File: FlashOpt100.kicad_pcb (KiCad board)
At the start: 2 copper layers, 16 x 38 mm, 8 parts, among them J1 Tandy_100_102_200_option_rom, J2 29C256, U1 29F010

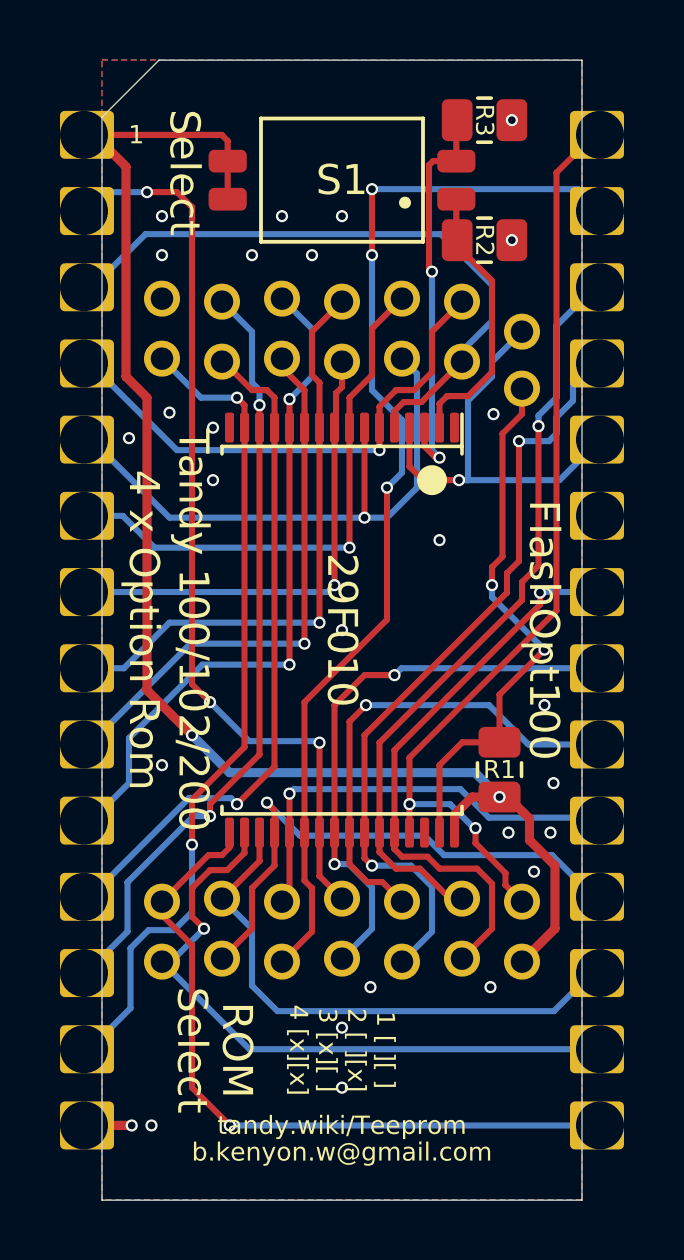
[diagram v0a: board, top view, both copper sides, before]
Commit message: adjust some footprints and remove flashopt100 programming adapter from readme
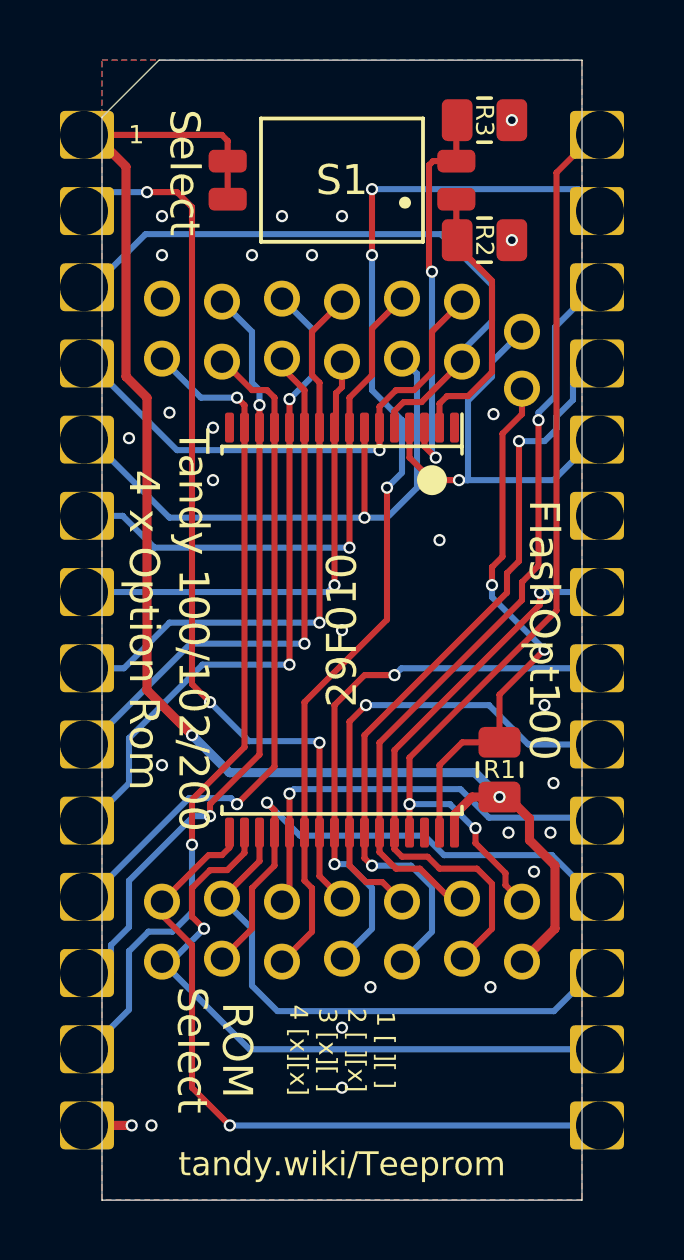
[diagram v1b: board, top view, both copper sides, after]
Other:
- board text removed: "b.kenyon.w@gmail.com"

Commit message: completely new FlashOpt100 and programming adapter
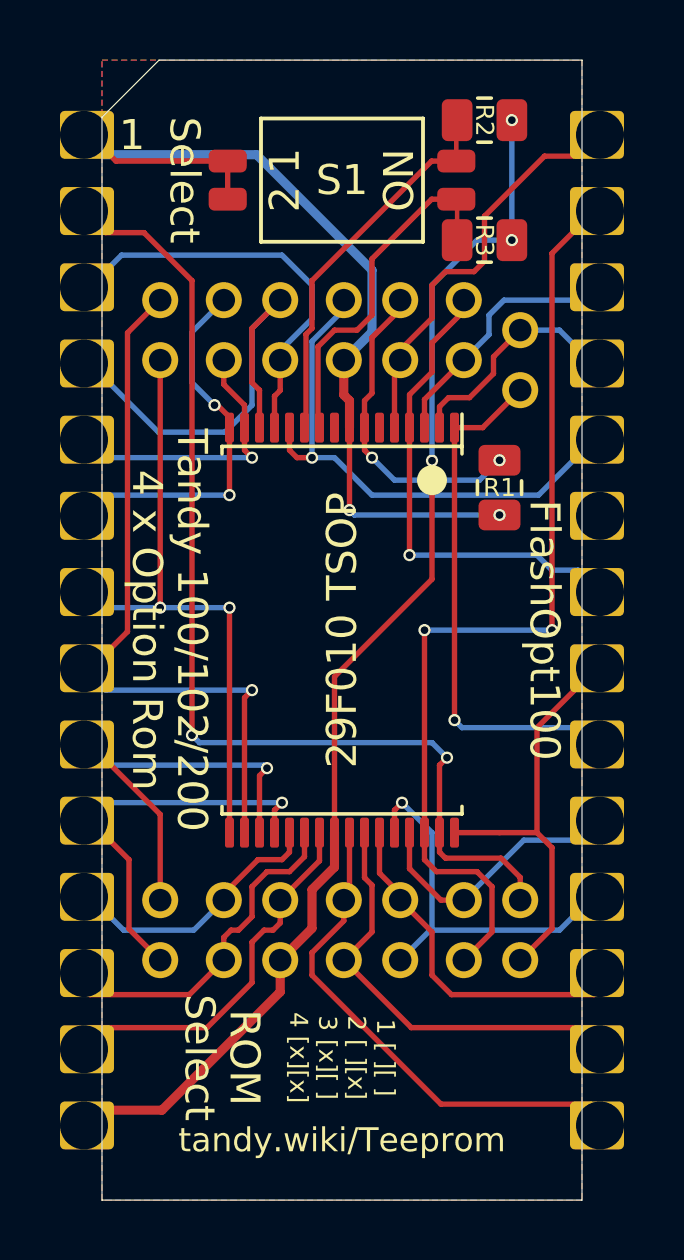
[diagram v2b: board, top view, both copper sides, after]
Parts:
- J2: value 29C256 -> FlashOpt100_PRG_4x7; footprint 000_LOCAL:4x7_prg_2.0mm_female_staggered -> 000_LOCAL:FlashOpt100_PRG_4x7_female_offset
- U1: value 29F010 -> 29F010 TSOP
- moved R1 9.40 mm to (152.5, 94.4)
- moved R2 4.00 mm to (152.0, 82.2)
- moved R3 4.00 mm to (152.0, 86.2)
- turned S1 to 0 degrees
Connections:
- J2 pad 1: /~WE -> /A11
- J2 pad 10: /A0 -> /A6
- J2 pad 11: /D0 -> /A5
- J2 pad 12: /D1 -> /A4
- J2 pad 13: /D2 -> /A3
- J2 pad 14: GND -> /A2
- J2 pad 15: /D3 -> /A1
- J2 pad 16: /D4 -> /A0
- J2 pad 17: /D5 -> /D0
- J2 pad 18: /D6 -> /D1
- J2 pad 19: /D7 -> /D2
- J2 pad 2: /A12 -> /A9
- J2 pad 20: /~CE -> GND
- J2 pad 21: /A10 -> /D3
- J2 pad 22: /~OE -> /D4
- J2 pad 23: /A11 -> /D5
- J2 pad 24: /A9 -> /D6
- J2 pad 25: /A8 -> /D7
- J2 pad 26: /A13 -> /~CE
- J2 pad 27: /A14 -> /A10
- J2 pad 28: VCC -> /~OE
- J2 pad 3: /A7 -> /A8
- J2 pad 4: /A6 -> /A13
- J2 pad 5: /A5 -> /A14
- J2 pad 6: /A4 -> /~WE
- J2 pad 7: /A3 -> VCC
- J2 pad 8: /A2 -> /A12
- J2 pad 9: /A1 -> /A7
- R2 pad 2: /A16 -> /A15
- R3 pad 2: /A15 -> /A16
- S1 pad 1A: /A16 -> VCC
- S1 pad 1B: VCC -> /A15
- S1 pad 2A: /A15 -> VCC
- S1 pad 2B: VCC -> /A16
- U1 pad 1: (no net) -> /A11
- U1 pad 10: /A2 -> /A16
- U1 pad 11: /A1 -> /A15
- U1 pad 12: /A0 -> /A12
- U1 pad 13: /D0 -> /A7
- U1 pad 14: /D1 -> /A6
- U1 pad 15: /D2 -> /A5
- U1 pad 16: GND -> /A4
- U1 pad 17: /D3 -> /A3
- U1 pad 18: /D4 -> /A2
- U1 pad 19: /D5 -> /A1
- U1 pad 2: /A16 -> /A9
- U1 pad 20: /D6 -> /A0
- U1 pad 21: /D7 -> /D0
- U1 pad 22: /~CE -> /D1
- U1 pad 23: /A10 -> /D2
- U1 pad 24: /~OE -> GND
- U1 pad 25: /A11 -> /D3
- U1 pad 26: /A9 -> /D4
- U1 pad 27: /A8 -> /D5
- U1 pad 28: /A13 -> /D6
- U1 pad 29: /A14 -> /D7
- U1 pad 3: /A15 -> /A8
- U1 pad 30: (no net) -> /~CE
- U1 pad 31: /~WE -> /A10
- U1 pad 32: VCC -> /~OE
- U1 pad 4: /A12 -> /A13
- U1 pad 5: /A7 -> /A14
- U1 pad 6: /A6 -> (no net)
- U1 pad 7: /A5 -> /~WE
- U1 pad 8: /A4 -> VCC
- U1 pad 9: /A3 -> (no net)
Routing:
- net GND: track 3.18 -> 41.3 mm, vias 27 -> 3
- net /A9: track 26.1 -> 7.89 mm, vias 2 -> 0
- net /A14: track 32.0 -> 13.8 mm, vias 2 -> 0
- net VCC: track 48.8 -> 31.4 mm
- net /A8: track 25.4 -> 8.73 mm, vias 1 -> 0
- net /D2: track 27.7 -> 13.0 mm, vias 2 -> 0
- net /D1: track 26.2 -> 11.9 mm, vias 2 -> 0
- net /D0: track 22.9 -> 9.16 mm, vias 1 -> 0
- net /A5: track 20.2 -> 9.49 mm
- net /A0: track 22.8 -> 13.8 mm, vias 2 -> 1
- net /A7: track 21.4 -> 13.7 mm
- net /~WE: track 18.1 -> 10.7 mm
- net /D3: track 24.2 -> 17.2 mm, vias 1 -> 0
- net /D5: track 18.5 -> 11.9 mm
- net /D4: track 22.1 -> 15.8 mm, vias 1 -> 0
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
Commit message: FlashOpt100 remove zone fill
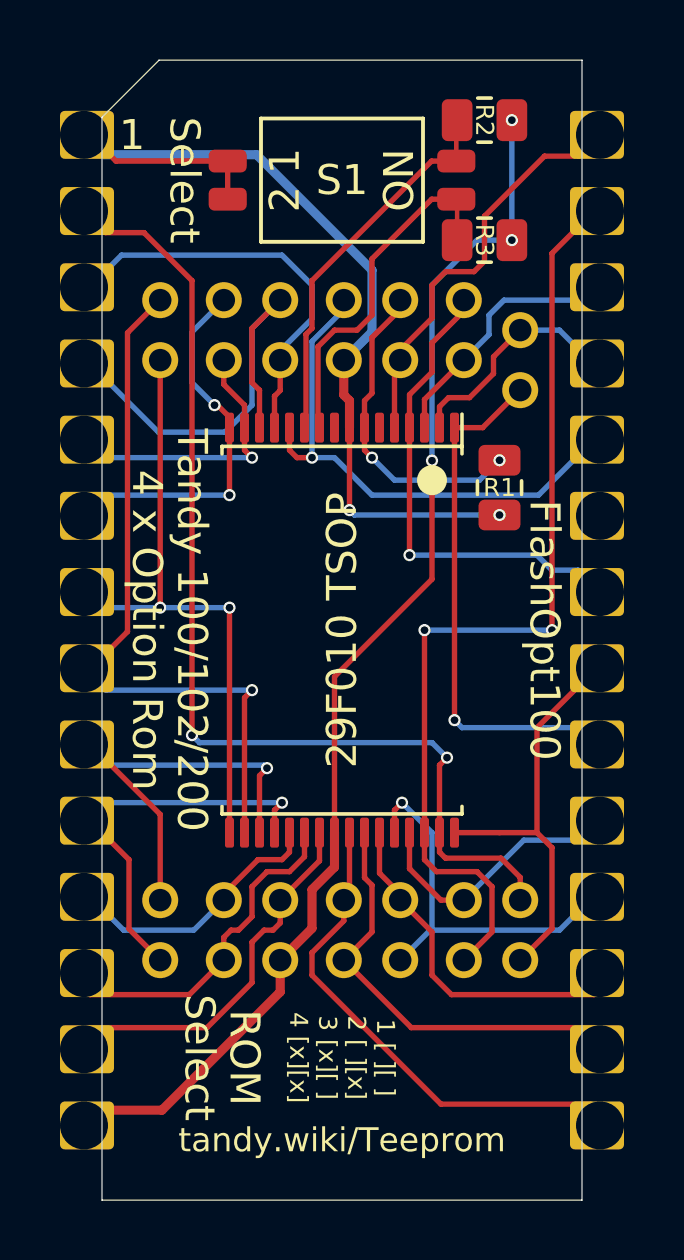
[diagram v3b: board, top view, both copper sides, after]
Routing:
- removed copper zone on B.Cu, net GND
- removed copper zone on F.Cu, net GND

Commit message: minor
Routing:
- net /A15: track 12.8 -> 14.2 mm
- net /A16: track 11.8 -> 10.9 mm
